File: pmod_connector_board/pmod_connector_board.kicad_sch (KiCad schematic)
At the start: 2 parts

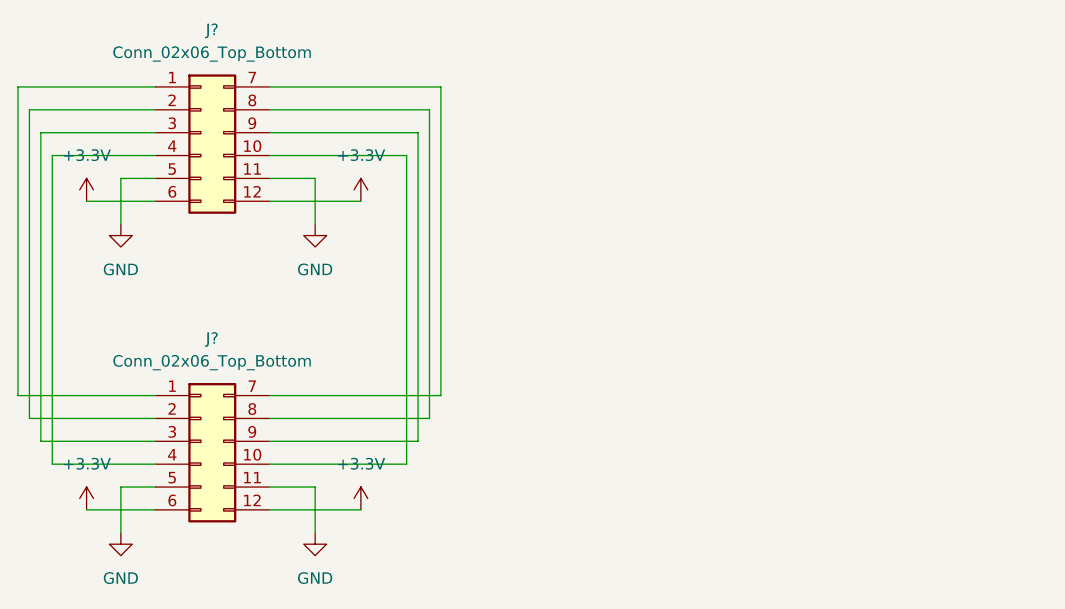
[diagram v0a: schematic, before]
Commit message: add board cut-out
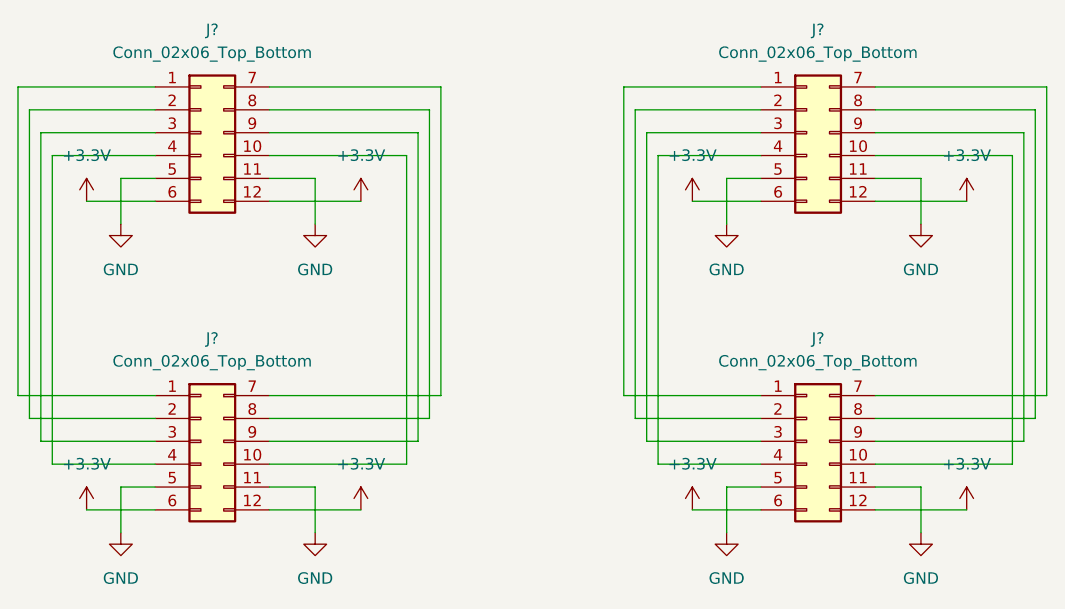
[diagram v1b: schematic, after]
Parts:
- added J? (x2): Conn_02x06_Top_Bottom, Connector_PinHeader_1.00mm:PinHeader_2x06_P1.00mm_Vertical, symbol Connector_Generic:Conn_02x06_Top_Bottom
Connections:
- net +3V3: now also J?.12 (Pin_12), J?.12 (Pin_12), J?.6 (Pin_6), J?.6 (Pin_6)
- net GND: now also J?.11 (Pin_11), J?.11 (Pin_11), J?.5 (Pin_5), J?.5 (Pin_5)
- new net: J?.1 (Pin_1), J?.1 (Pin_1)
- new net: J?.10 (Pin_10), J?.10 (Pin_10)
- new net: J?.2 (Pin_2), J?.2 (Pin_2)
- new net: J?.3 (Pin_3), J?.3 (Pin_3)
- new net: J?.4 (Pin_4), J?.4 (Pin_4)
- new net: J?.7 (Pin_7), J?.7 (Pin_7)
- new net: J?.8 (Pin_8), J?.8 (Pin_8)
- new net: J?.9 (Pin_9), J?.9 (Pin_9)

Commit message: finish PMOD connector PCB
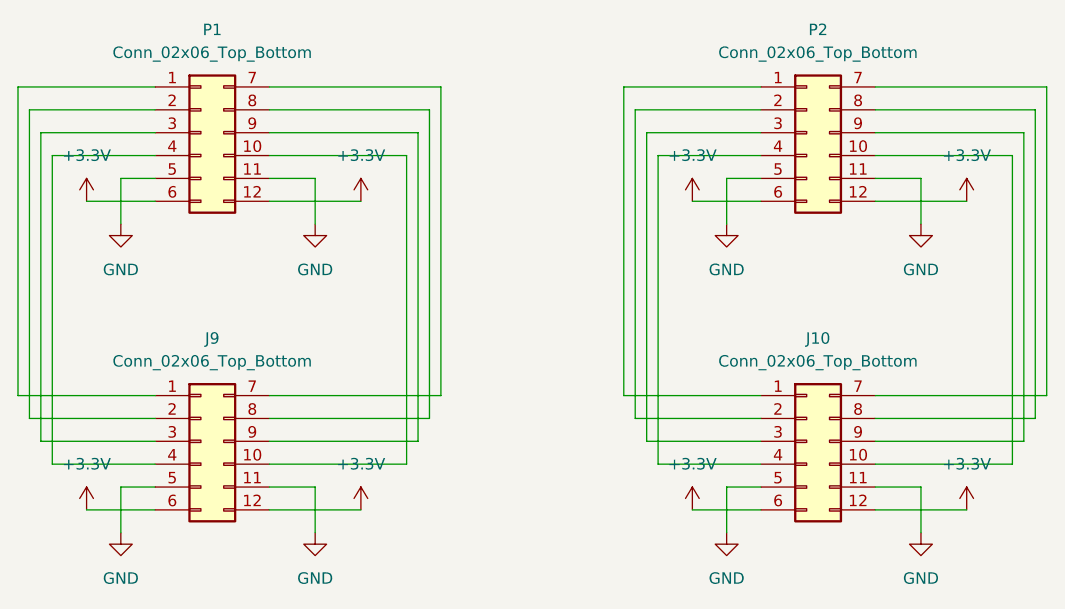
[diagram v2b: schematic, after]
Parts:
- gave numbers to parts that had none: 4
